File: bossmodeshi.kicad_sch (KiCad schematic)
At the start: 127 parts, among them Q1 FZT853TA, Q2 PSMN3R7-100BSE, Q3 PSMN3R7-100BSE, Q4 PSMN3R7-100BSE, Q5 PSMN3R7-100BSE, Q6 Q_PMOS_GDS, U10 SQ1464EEH-T1_GE3, U11 MP2790DFP-0000-T, U5 SQ1464EEH-T1_GE3, U6 SQ1464EEH-T1_GE3, U7 SQ1464EEH-T1_GE3, U8 SQ1464EEH-T1_GE3, U9 SQ1464EEH-T1_GE3

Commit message: Finalizing BOM
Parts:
- R37: renamed from R33; Supplier_2 P/N C105578 -> C105578
- R_CHG_DRIVER1, R_CHG_MG1, R_CHG_MG2, R_DSG_DRIVER1, R_DSG_MG1, R_DSG_MG2, R_SRN_FLT1, R_SRP_FLT1: Supplier_2 P/N C844725 -> C844725
- renumbered R45 to R21, R44 to R22, R46 to R23, R47 to R24, R48 to R25, R49 to R26, R23 to R27, R24 to R28, R25 to R29, R26 to R30, R27 to R31, R28 to R32, R29 to R33, R30 to R34, R31 to R35, R32 to R36, R34 to R38, R35 to R39, R36 to R40, R37 to R41, R38 to R42, R39 to R43, R40 to R44, R41 to R45, R42 to R46, R43 to R47, TP12 to TP11, TP13 to TP12, TP14 to TP13, TP11 to TP14, U11 to U10, U5 to U4, U6 to U5, U7 to U6, U8 to U7, U9 to U8, U10 to U9

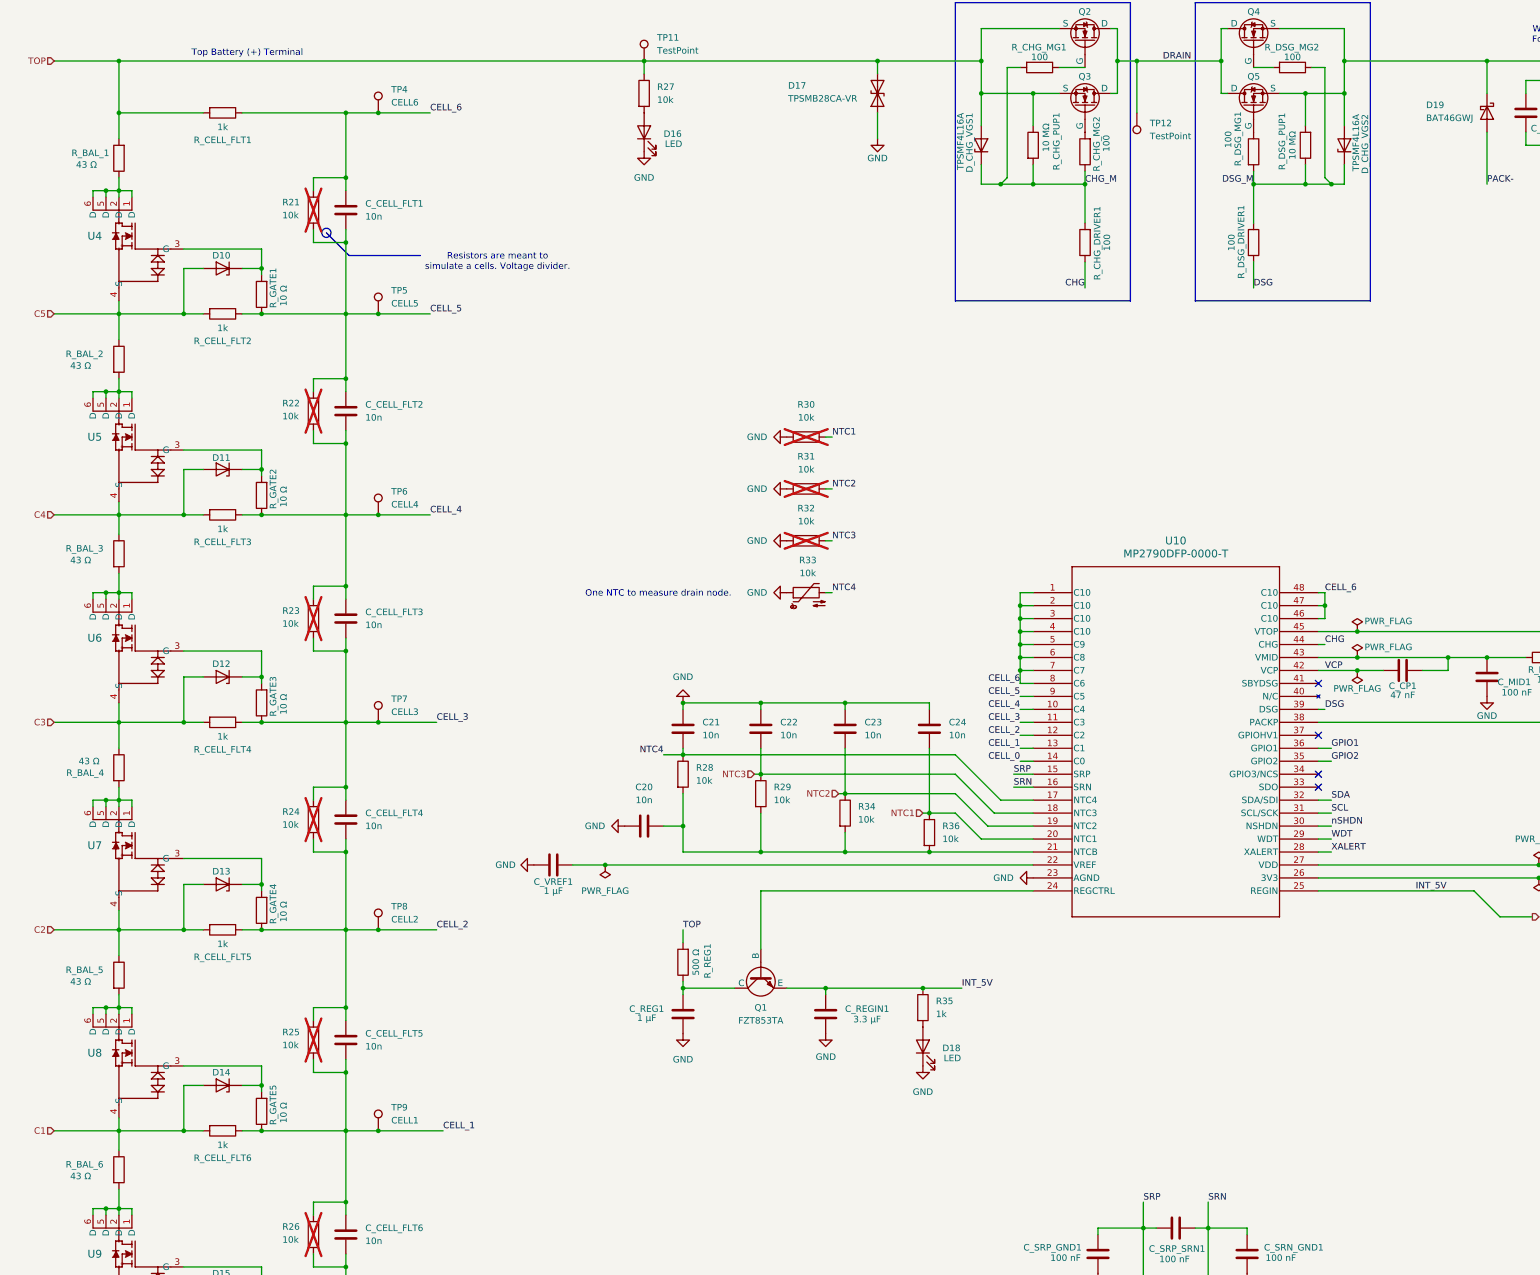
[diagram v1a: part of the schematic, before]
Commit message: rev3: nSHDN wake divider (1M/200k, 10k series to GPIO11), R_REG 100R 2512, 51R balance resistors, NTC ground resistors DNP, SMBJ28CA on TOP, BOM updates
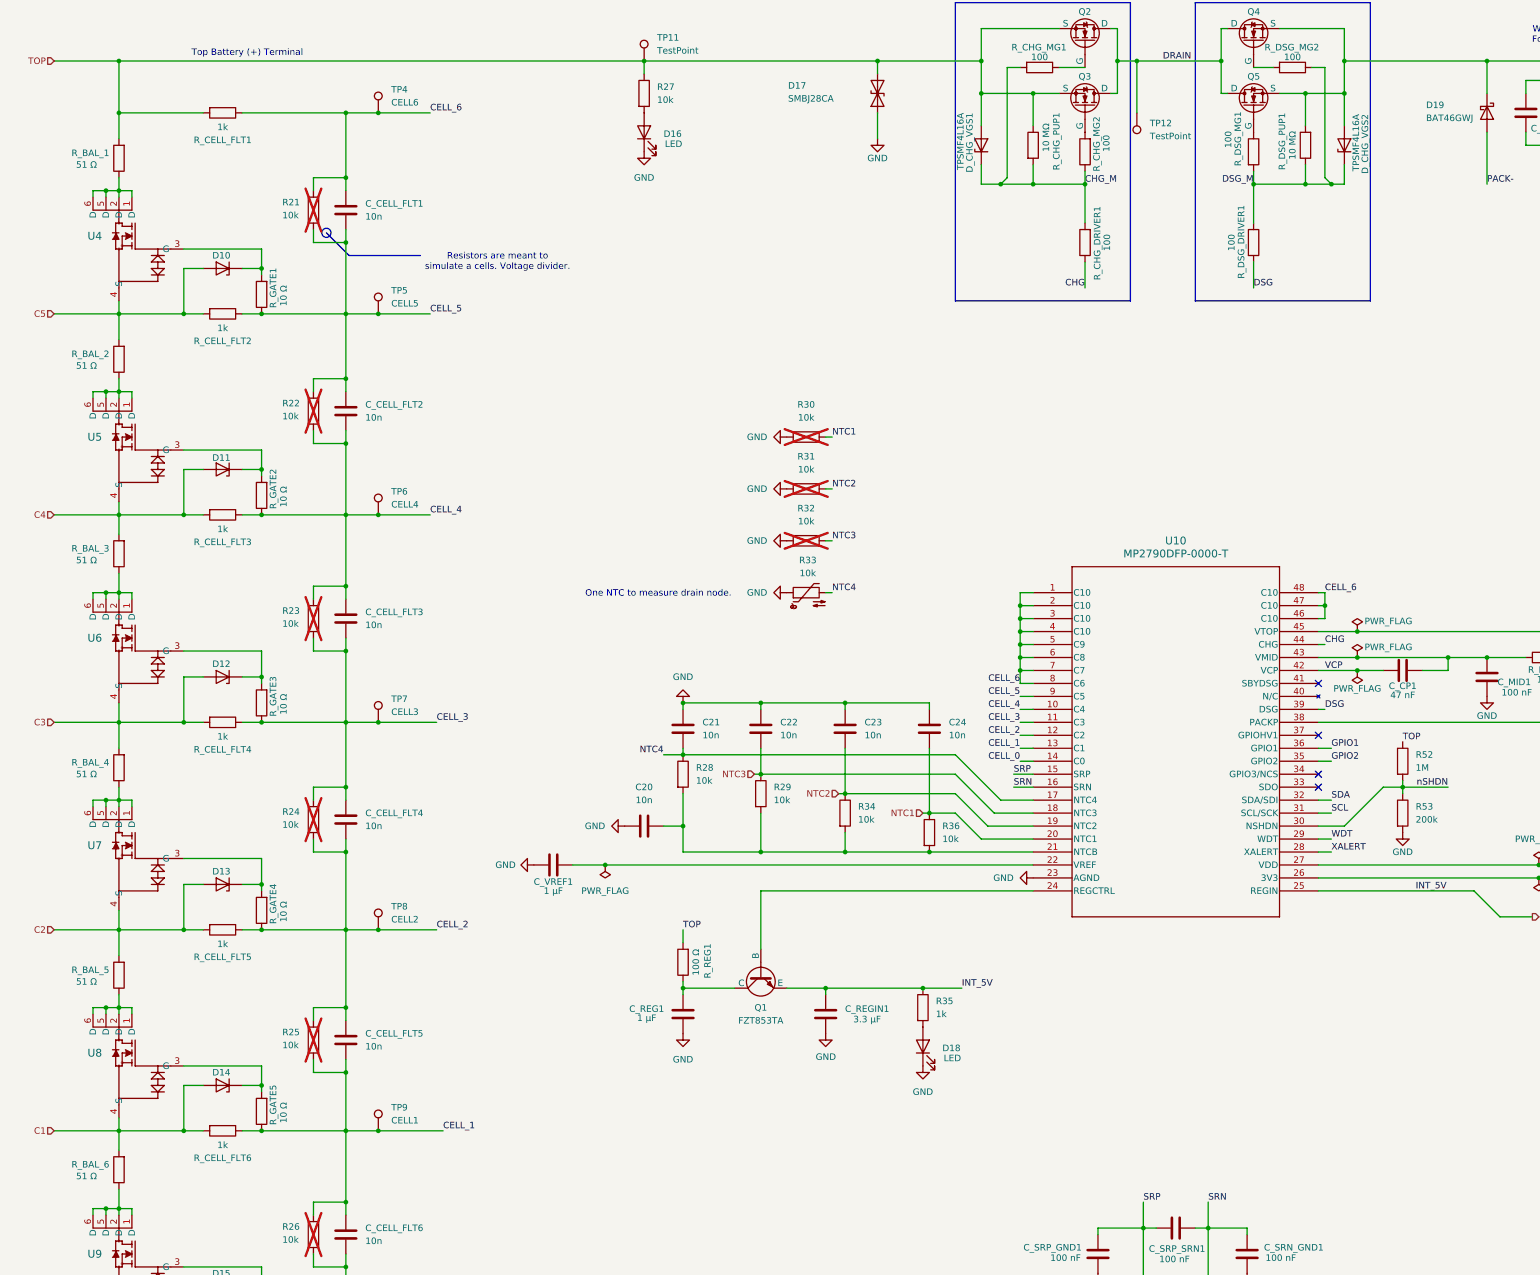
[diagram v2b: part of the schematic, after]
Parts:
- added R52: 1M, Resistor_SMD:R_0603_1608Metric, symbol Device:R
- added R53: 200k, Resistor_SMD:R_0603_1608Metric, symbol Device:R
- D17: value TPSMB28CA-VR -> SMBJ28CA; Mfr Littelfuse Inc. -> Littelfuse; Mfr P/N TPSMB28CA-VR -> SMBJ28CA; Supplier_1 Digikey -> (none); Supplier_1 P/N TPSMB28CA-VRTR-ND -> (none); Supplier_1 Price @ Qty 1 -> (none); Supplier_1 Unit Price 0.23000 -> (none); Supplier_2 P/N (none) -> C151259
- R_BAL_1, R_BAL_2, R_BAL_3, R_BAL_4, R_BAL_5, R_BAL_6: value 43 Ω -> 51 Ω; Mfr Vishay Intertech -> YAGEO; Mfr P/N CRCW120643R0FKEAHP -> SR1206FR-7W51RL; Supplier_2 P/N C4017025 -> C873963
- R_REG1: value 500 Ω -> 100 Ω; footprint Resistor_SMD:R_1206_3216Metric -> Resistor_SMD:R_2512_6332Metric; Mfr Vishay Intertech -> UNI-ROYAL(Uniroyal Elec); Mfr P/N TNPW1206100RBEEA -> 25121WJ0101T4E; Supplier_2 P/N C844470 -> C24920
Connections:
- net C1: now also R_BAL_6.2; no longer R_BAL_6.1
- net C2: now also R_BAL_5.2; no longer R_BAL_5.1
- net C3: now also R_BAL_4.2; no longer R_BAL_4.1
- net C4: now also R_BAL_3.2; no longer R_BAL_3.1
- net C5: now also R_BAL_2.2; no longer R_BAL_2.1
- net GND: now also R53.2
- net TOP: now also R52.1
- net nSHDN: now also R52.2, R53.1
- net at U9.1 (D), U9.2 (D), U9.5 (D)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: now also R_BAL_6.1; no longer R_BAL_6.2
- net at U8.1 (D), U8.2 (D), U8.5 (D)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: now also R_BAL_5.1; no longer R_BAL_5.2
- net at U7.1 (D), U7.2 (D), U7.5 (D)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: now also R_BAL_4.1; no longer R_BAL_4.2
- net at U5.1 (D), U5.2 (D), U5.5 (D)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: now also R_BAL_2.1; no longer R_BAL_2.2
- net at U6.1 (D), U6.2 (D), U6.5 (D)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: now also R_BAL_3.1; no longer R_BAL_3.2
